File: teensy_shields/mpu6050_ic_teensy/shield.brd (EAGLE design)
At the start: 26.6 x 60.6 mm, 6 parts

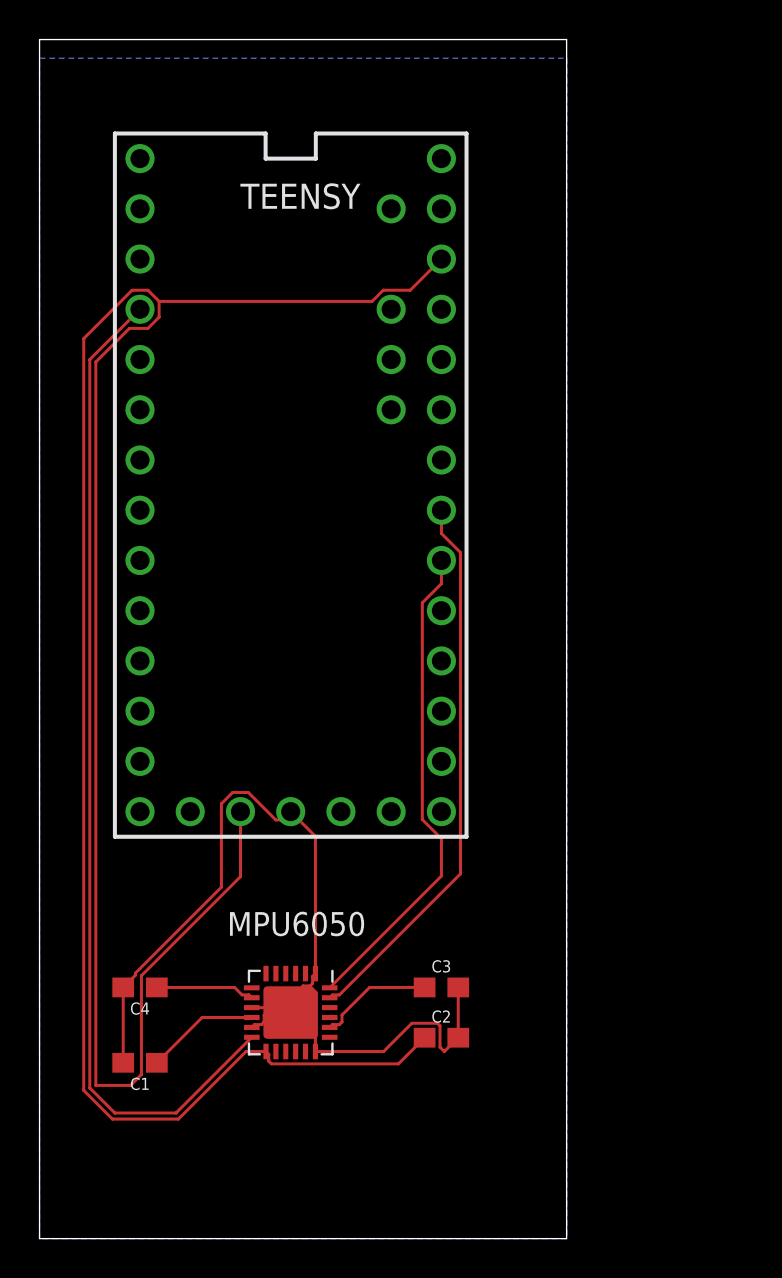
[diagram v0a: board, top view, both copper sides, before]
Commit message: Switched files
Corrected file directories
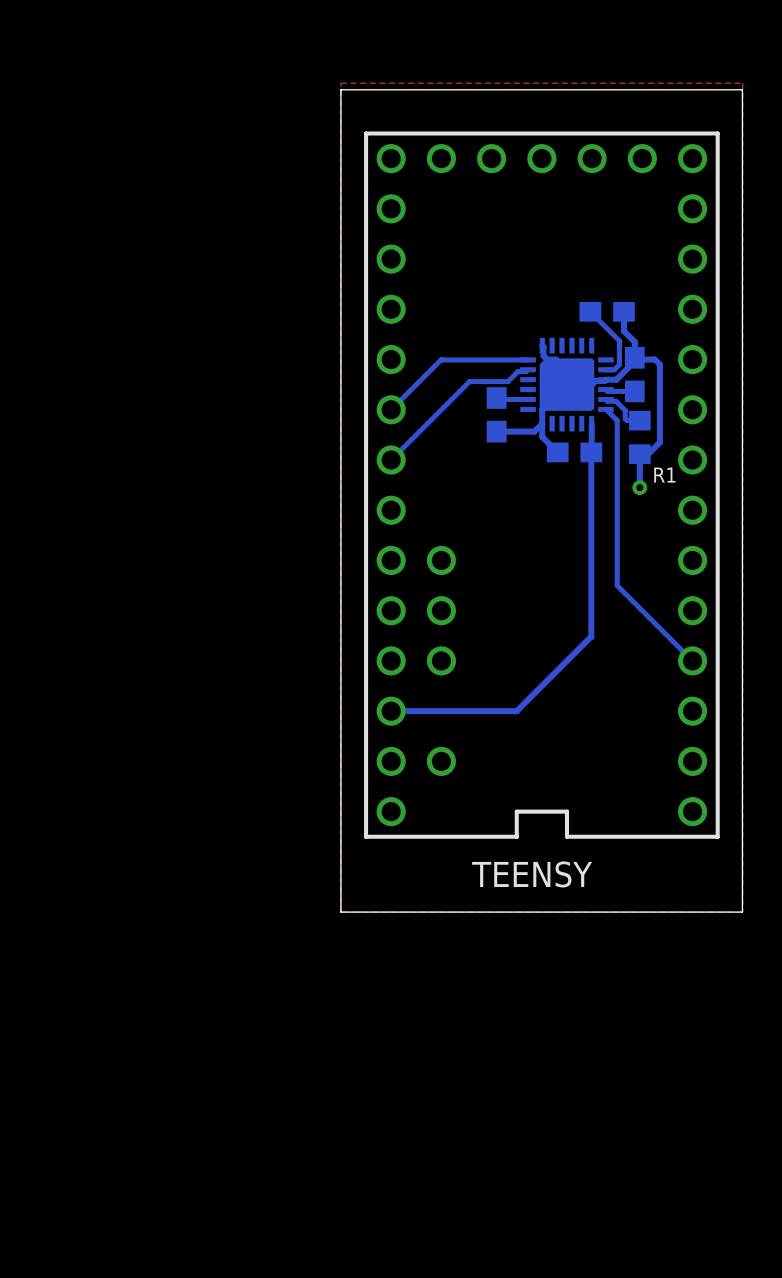
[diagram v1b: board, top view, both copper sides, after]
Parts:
- added R1: (no value), eagle-ltspice:R0603
- moved C1 42.9 mm to (35.2, 83.1), flipped to the bottom, turned to 90 degrees
- moved C4 41.5 mm to (33.8, 86.2), flipped to the bottom
- moved MPU6050 34.7 mm to (31.8, 82.5), flipped to the bottom
- moved C2 30.3 mm to (32.1, 79.1), flipped to the bottom
- moved C3 29.1 mm to (28.2, 81.0), flipped to the bottom, turned to 270 degrees
- moved TEENSY 12.7 mm to (30.5, 77.5), turned to 180 degrees
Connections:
- new net N$4: MPU6050.11, R1.1
- net GND: now also R1.2; no longer MPU6050.11
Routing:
- net VCC: track 137.9 -> 22.5 mm
- net INT: track 50.7 -> 14.5 mm
- net GND: track 50.5 -> 24.4 mm, vias 0 -> 1
- net SCL: track 28.0 -> 8.81 mm
- net SDA: track 24.7 -> 7.98 mm
- net N$2: track 5.75 -> 1.50 mm
- net N$1: track 5.84 -> 1.62 mm
- net N$4: track 0.00 -> 2.40 mm
- net N$3: track 5.02 -> 4.08 mm
- added copper zone on layer 1, net GND
- removed copper zone on layer 16, net GND
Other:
- board size 26.6 x 60.6 mm -> 20.3 x 41.6 mm
- board text added: "R1"
